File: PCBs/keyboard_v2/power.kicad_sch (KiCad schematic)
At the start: 15 parts, among them IC501 ADP5360ACBZ-2-R7, U501 MAX9938TEBS+TG45

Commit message: V2 progress
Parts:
- renumbered C501 to C1401, C502 to C1402, C503 to C1403, C504 to C1404, C505 to C1405, C506 to C1406, C507 to C1407, C508 to C1408, IC501 to IC1401, L501 to L1401, L502 to L1402, R501 to R1401, R502 to R1402, R503 to R1403, U501 to U1401
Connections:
- net I2C.SCL renamed SCL
- net I2C.SDA renamed SDA
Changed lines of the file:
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@@
 		(at 116.84 121.92)
 	)
-	(bus_entry
-		(at 101.6 104.14)
-		(size 2.54 2.54)
-		(stroke
-			(width 0)
-			(type default)
-		)
-	)
-	(bus_entry
-		(at 101.6 101.6)
-		(size 2.54 2.54)
-		(stroke
-			(width 0)
-			(type default)
-		)
-	)
 	(wire
 		(pts
@@
 	(wire
 		(pts
-			(xy 88.9 109.22) (xy 116.84 109.22)
+			(xy 104.14 109.22) (xy 116.84 109.22)
 		)
 		(stroke
@@
 		)
 	)
-	(bus
-		(pts
-			(xy 101.6 101.6) (xy 101.6 104.14)
-		)
-		(stroke
-			(width 0)
-			(type default)
-		)
-	)
 	(wire
 		(pts
@@
 		)
 	)
-	(bus
-		(pts
-			(xy 101.6 101.6) (xy 88.9 101.6)
-		)
-		(stroke
-			(width 0)
-			(type default)
-		)
-	)
 	(wire
 		(pts
@@
 	(wire
 		(pts
-			(xy 88.9 111.76) (xy 116.84 111.76)
+			(xy 104.14 111.76) (xy 116.84 111.76)
 		)
 		(stroke
@@
 	(text "I2C Address: 0x46"
 		(exclude_from_sim no)
-		(at 60.96 99.06 0)
+		(at 68.58 101.6 0)
 		(effects
 			(font
@@
 	(text "INT needs to be\npulled up by host"
 		(exclude_from_sim no)
-		(at 60.96 111.76 0)
+		(at 68.58 114.3 0)
 		(effects
 			(font
@@
 	(text "I2C Pullups on\nSTM32 sheet"
 		(exclude_from_sim no)
-		(at 60.96 104.14 0)
+		(at 68.58 106.68 0)
 		(effects
 			(font
@@
 		)
 	)
-	(label "I2C{I2C}"
-		(at 99.06 101.6 180)
-		(fields_autoplaced yes)
-		(effects
-			(font
-				(size 1.27 1.27)
-			)
-			(justify right bottom)
-		)
-	)
 	(label "I2C.SCL"
 		(at 106.68 104.14 0)
@@
 	(hierarchical_label "INT"
 		(shape output)
-		(at 88.9 109.22 180)
+		(at 104.14 109.22 180)
 		(fields_autoplaced yes)
 		(effects
@@
 		)
 	)
-	(hierarchical_label "I2C"
-		(shape bidirectional)
-		(at 88.9 101.6 180)
+	(hierarchical_label "SDA"
+		(shape input)
+		(at 104.14 106.68 180)
 		(fields_autoplaced yes)
 		(effects
@@
 			(justify right)
 		)
-		(property "DSI" "DSI"
-			(at 88.9 102.87 0)
-			(effects
-				(font
-					(size 1.27 1.27)
-					(italic yes)
-				)
-				(justify right)
-				(hide yes)
-			)
-		)
 	)
 	(hierarchical_label "ENCHG"
 		(shape input)
-		(at 88.9 111.76 180)
+		(at 104.14 111.76 180)
+		(fields_autoplaced yes)
+		(effects
+			(font
+				(size 1.27 1.27)
+			)
+			(justify right)
+		)
+	)
+	(hierarchical_label "SCL"
+		(shape bidirectional)
+		(at 104.14 104.14 180)
 		(fields_autoplaced yes)
 		(effects
@@
 		(on_board yes)
 		(dnp no)
-		(property "Reference" "R503"
+		(property "Reference" "R1403"
 			(at 185.42 55.88 90)
 			(effects
@@
 		(on_board yes)
 		(dnp no)
-		(property "Reference" "IC501"
+		(property "Reference" "IC1401"
 			(at 142.24 53.34 0)
 			(effects
@@
 		(dnp no)
 		(fields_autoplaced yes)
-		(property "Reference" "L501"
+		(property "Reference" "L1401"
 			(at 180.34 81.28 90)
 			(effects
@@
 		(dnp no)
 		(fields_autoplaced yes)
-		(property "Reference" "#PWR0503"
+		(property "Reference" "#PWR01403"
 			(at 88.9 82.55 0)
 			(effects
@@
 		(on_board yes)
 		(dnp no)
-		(property "Reference" "C501"
+		(property "Reference" "C1401"
 			(at 86.36 67.3163 0)
 			(effects
@@
 		(dnp no)
 		(fields_autoplaced yes)
-		(property "Reference" "L502"
+		(property "Reference" "L1402"
 			(at 181.61 113.03 0)
 			(effects
@@
 		(on_board yes)
 		(dnp no)
-		(property "Reference" "C502"
+		(property "Reference" "C1402"
 			(at 96.52 67.3163 0)
 			(effects
@@
 		(dnp no)
 		(fields_autoplaced yes)
-		(property "Reference" "#PWR0501"
+		(property "Reference" "#PWR01401"
 			(at 88.9 62.23 0)
 			(effects
@@
 		(dnp no)
 		(fields_autoplaced yes)
-		(property "Reference" "#PWR0512"
+		(property "Reference" "#PWR01412"
 			(at 195.58 85.09 0)
 			(effects
@@
 		(on_board yes)
 		(dnp no)
-		(property "Reference" "R501"
+		(property "Reference" "R1401"
 			(at 109.22 67.31 0)
 			(effects
@@
 		(on_board yes)
 		(dnp no)
-		(property "Reference" "#PWR0510"
+		(property "Reference" "#PWR01410"
 			(at 193.04 102.87 0)
 			(effects
@@
 		(dnp no)
 		(fields_autoplaced yes)
-		(property "Reference" "#PWR0514"
+		(property "Reference" "#PWR01414"
 			(at 203.2 87.63 0)
 			(effects
@@
 		(on_board yes)
 		(dnp no)
-		(property "Reference" "C503"
+		(property "Reference" "C1403"
 			(at 109.22 87.6363 0)
 			(effects
@@
 		(dnp no)
 		(fields_autoplaced yes)
-		(property "Reference" "#PWR0511"
+		(property "Reference" "#PWR01411"
 			(at 193.04 120.65 0)
 			(effects
@@
 		(on_board yes)
 		(dnp no)
-		(property "Reference" "C508"
+		(property "Reference" "C1408"
 			(at 198.12 69.8563 0)
 			(effects
@@
 		(dnp no)
 		(fields_autoplaced yes)
-		(property "Reference" "#PWR0509"
+		(property "Reference" "#PWR01409"
 			(at 170.18 148.59 0)
 			(effects
@@
 		(on_board yes)
 		(dnp no)
-		(property "Reference" "R502"
+		(property "Reference" "R1402"
 			(at 111.76 133.35 0)
 			(effects
@@
 		(dnp no)
 		(fields_autoplaced yes)
-		(property "Reference" "#PWR0506"
+		(property "Reference" "#PWR01406"
 			(at 111.76 100.33 0)
 			(effects
@@
 		(dnp no)
 		(fields_autoplaced yes)
-		(property "Reference" "#PWR0507"
+		(property "Reference" "#PWR01407"
 			(at 114.3 148.59 0)
 			(effects
@@
 		(on_board yes)
 		(dnp no)
-		(property "Reference" "C507"
+		(property "Reference" "C1407"
 			(at 195.58 107.9563 0)
 			(effects
@@
 		(dnp no)
 		(fields_autoplaced yes)
-		(property "Reference" "#PWR0515"
+		(property "Reference" "#PWR01415"
 			(at 203.2 105.41 0)
 			(effects
@@
 		(dnp no)
 		(fields_autoplaced yes)
-		(property "Reference" "#PWR0505"
+		(property "Reference" "#PWR01405"
 			(at 109.22 85.09 0)
 			(effects
@@
 		(dnp no)
 		(fields_autoplaced yes)
-		(property "Reference" "#PWR0504"
+		(property "Reference" "#PWR01404"
 			(at 99.06 62.23 0)
 			(effects
@@
 		(on_board yes)
 		(dnp no)
-		(property "Reference" "#PWR0508"
+		(property "Reference" "#PWR01408"
 			(at 166.37 124.46 0)
 			(effects
@@
 		(dnp no)
 		(fields_autoplaced yes)
-		(property "Reference" "#PWR0513"
+		(property "Reference" "#PWR01413"
 			(at 203.2 64.77 0)
 			(effects
@@
 		(dnp no)
 		(fields_autoplaced yes)
-		(property "Reference" "U501"
+		(property "Reference" "U1401"
 			(at 203.2 38.1 0)
 			(effects
@@
 		(dnp no)
 		(fields_autoplaced yes)
-		(property "Reference" "#PWR0516"
+		(property "Reference" "#PWR01416"
 			(at 210.82 67.31 0)
 			(effects
@@
 		(on_board yes)
 		(dnp no)
-		(property "Reference" "C506"
+		(property "Reference" "C1406"
 			(at 195.58 90.1763 0)
 			(effects
@@
 		(on_board yes)
 		(dnp no)
-		(property "Reference" "C505"
+		(property "Reference" "C1405"
 			(at 187.96 69.8563 0)
 			(effects
@@
 		(on_board yes)
 		(dnp no)
-		(property "Reference" "C504"
+		(property "Reference" "C1404"
 			(at 177.8 69.8563 0)
 			(effects

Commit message: V2 Schematic mostly done
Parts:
- added Q1401: DMP2104LP-7, keyboard_footprints:DMP2104LP7, symbol DMP2104LP-7:DMP2104LP-7
- added SW502: PCM12SMTBR, PCM12SMTBR, symbol PCM12SMTBR:PCM12SMTBR
- added TP1401, TP1402: 3mm, TestPoint:TestPoint_Pad_D3.0mm, symbol Connector:TestPoint_Small
- IC1401: footprint watch_footprints:ADP5360ACBZ1R7 -> keyboard_footprints:ADP5360ACBZ1R7
- U1401: footprint watch_footprints:BGA4C50P2X2_100X100X67 -> keyboard_footprints:BGA4C50P2X2_100X100X67
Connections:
- net +VBAT: now also Q1401.2 (D)
- net GND: now also SW502.3 (C), SW502.MP1, SW502.MP2, SW502.MP3, SW502.MP4, TP1402.1
- net BTN renamed MR
- new net BAT: Q1401.3 (S), SW502.1 (A), TP1401.1
- new net BAT_SW: Q1401.1 (G), SW502.2 (B)
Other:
- moved on the sheet: C1401, C1402, C1403, C1404, C1405, C1406, C1407, C1408, IC1401, L1401, L1402, R1401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

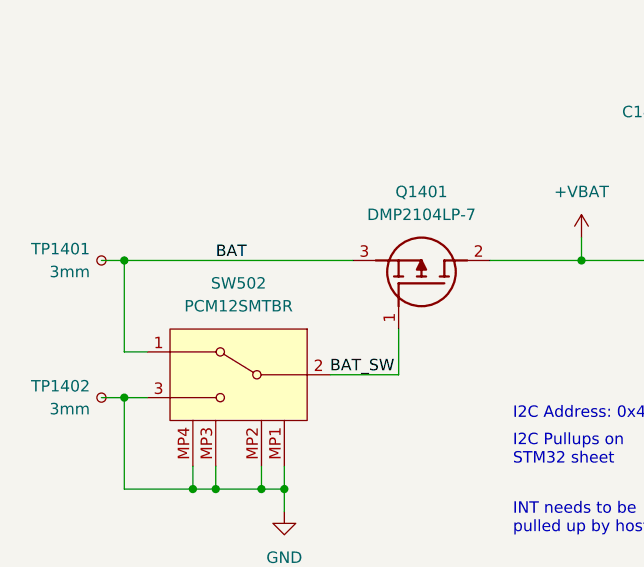
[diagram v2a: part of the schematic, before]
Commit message: Added debug header footprint
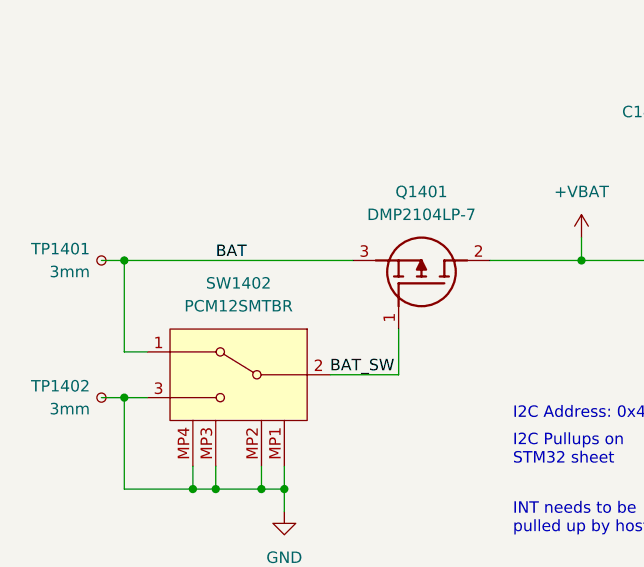
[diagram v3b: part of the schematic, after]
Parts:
- renumbered SW502 to SW1402
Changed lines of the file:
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@@
 		(dnp no)
 		(fields_autoplaced yes)
-		(property "Reference" "#PWR0502"
+		(property "Reference" "#PWR01402"
 			(at 58.42 118.11 0)
 			(effects
@@
 		(on_board yes)
 		(dnp no)
-		(property "Reference" "SW502"
+		(property "Reference" "SW1402"
 			(at 53.34 86.36 0)
 			(effects
